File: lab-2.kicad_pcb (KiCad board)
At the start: 2 copper layers, 29.7 x 59.5 mm, 30 parts, among them J1 Conn_01x04_Pin, J2 USB_C_Receptacle, SW1 NRST, SW2 BOOT, U1 LM66100DCK, U2 LM66100DCK, U3 STM32F405RGTx, U4 MCP1700x-120xxMB, Y1 8 MHz

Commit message: Added 2 new layers + GPIO port A (4 pins)
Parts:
- added J3: Conn_PORT C, Connector_PinHeader_2.54mm:PinHeader_1x04_P2.54mm_Vertical, F.Cu at (170.3, 117.5)
- added J4: Conn_GND, Connector_PinHeader_2.54mm:PinHeader_1x04_P2.54mm_Vertical, F.Cu at (170.3, 90.8)
- J1: value Conn_01x04_Pin -> Conn_SWD
- turned U2 to -90 degrees
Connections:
- U3 pad 37: unconnected-(U3-PC6-Pad37) -> /GPIOC_6
- U3 pad 38: unconnected-(U3-PC7-Pad38) -> /GPIOC_7
- U3 pad 39: unconnected-(U3-PC8-Pad39) -> /GPIOC_8
- U3 pad 40: unconnected-(U3-PC9-Pad40) -> /GPIOC_9
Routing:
- net +3.3V: track 100.4 -> 22.5 mm, vias 0 -> 10
- net /GPIOC_9: track 0.00 -> 32.4 mm, vias 0 -> 2
- net /GPIOC_8: track 0.00 -> 28.1 mm, vias 0 -> 1
- net /GPIOC_7: track 0.00 -> 25.5 mm, vias 0 -> 2
- net /GPIOC_6: track 0.00 -> 22.1 mm, vias 0 -> 1
- net /SWCLK: track 22.9 -> 19.3 mm
- net +3.3V_STLINK: track 8.61 -> 6.46 mm
- net GND: track 38.0 -> 40.1 mm
- net +3.3V_LDO: track 15.0 -> 13.2 mm
- net /BOOT0: track 21.6 -> 20.6 mm, vias 2 -> 0
- net /SWDIO: track 17.3 -> 16.6 mm, vias 2 -> 0
- added copper zone on In2.Cu, net +3.3V
- added copper zone on In1.Cu, net GND
- removed copper zone on B.Cu, net GND
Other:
- copper layers 2 -> 4

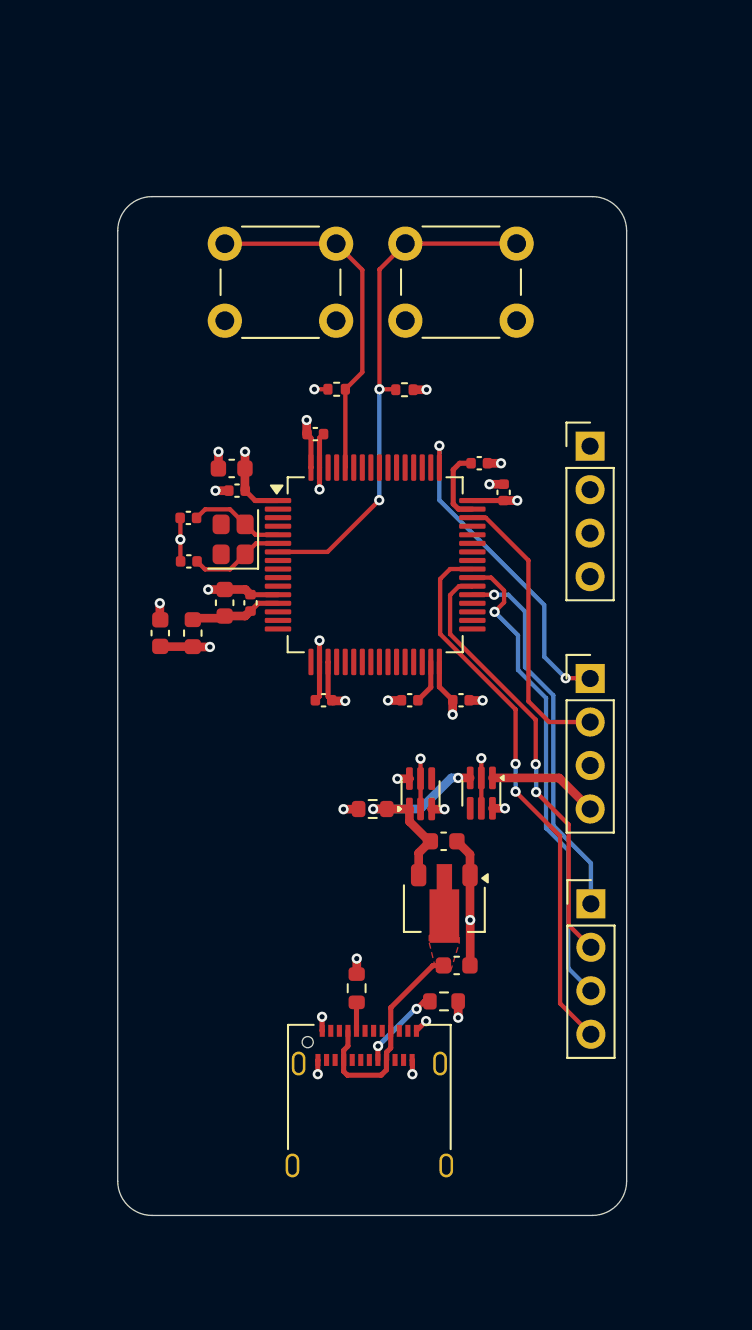
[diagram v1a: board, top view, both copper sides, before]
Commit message: add USER button and LEDs
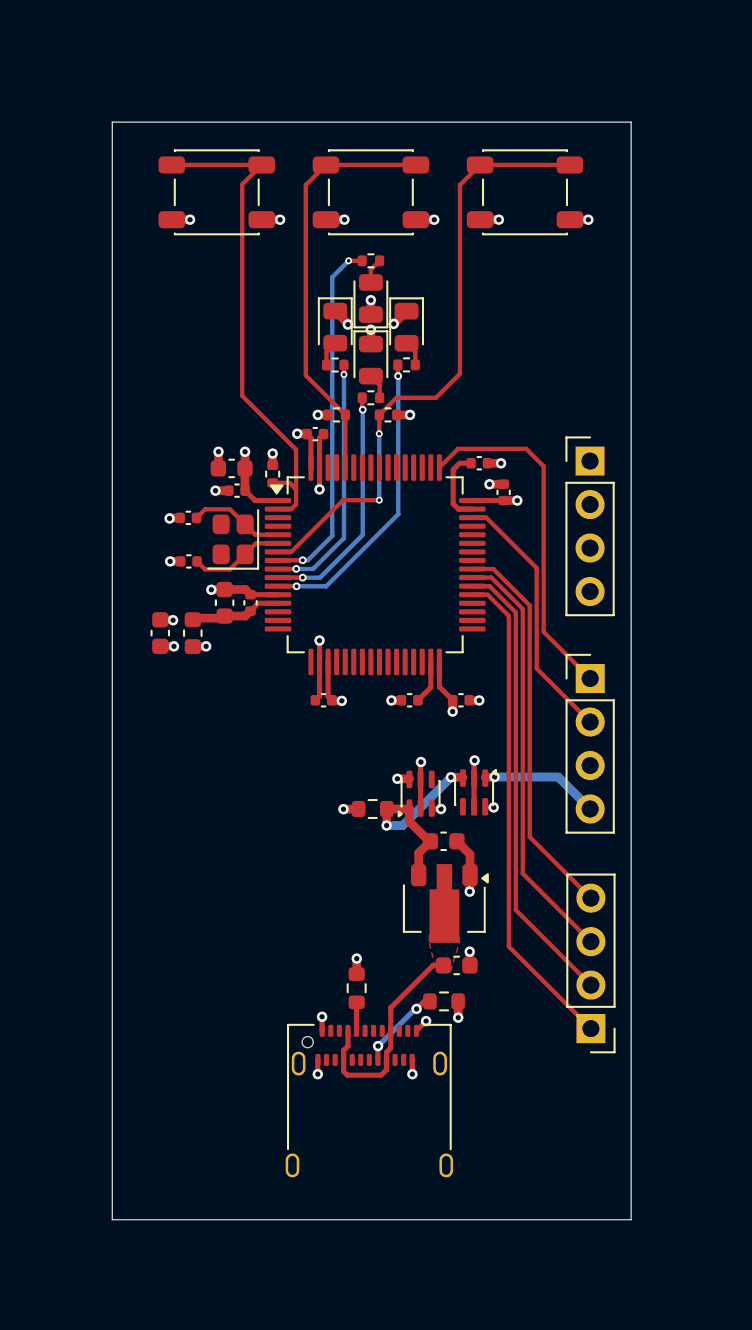
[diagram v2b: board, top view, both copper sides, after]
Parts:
- added D1: RED, LED_SMD:LED_0805_2012Metric, F.Cu at (157.5, 82.2)
- added D2: YELLOW, LED_SMD:LED_0805_2012Metric, F.Cu at (155.4, 83.9)
- added D3: GREEN, LED_SMD:LED_0805_2012Metric, F.Cu at (157.5, 85.8)
- added D4: BLUE, LED_SMD:LED_0805_2012Metric, F.Cu at (159.6, 83.9)
- added R10: 39, Resistor_SMD:R_0402_1005Metric, F.Cu at (159.6, 86.1)
- added R4: 130, Resistor_SMD:R_0402_1005Metric, F.Cu at (157.5, 80.0)
- added R7: 10k, Resistor_SMD:R_0402_1005Metric, F.Cu at (151.8, 92.5)
- added R8: 130, Resistor_SMD:R_0402_1005Metric, F.Cu at (155.4, 86.1)
- added R9: 56, Resistor_SMD:R_0402_1005Metric, F.Cu at (157.5, 88.0)
- added SW3: USER, Button_Switch_SMD:SW_SPST_PTS647_Sx38, F.Cu at (148.5, 76.0)
- SW1, SW2: footprint Button_Switch_THT:SW_PUSH_6mm_H4.3mm -> Button_Switch_SMD:SW_SPST_PTS647_Sx38
- moved SW2 9.04 mm to (157.5, 76.0)
- moved SW1 7.60 mm to (166.5, 76.0)
- moved J3 7.29 mm to (170.3, 124.8), turned to 180 degrees
- moved R5 1.76 mm to (158.5, 89.0)
- moved R6 1.50 mm to (155.5, 89.0)
- moved J4 0.87 mm to (170.3, 91.7)
- moved U2 0.43 mm to (163.5, 111.0)
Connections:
- U3 pad 10: unconnected-(U3-PC2-Pad10) -> /GREEN_LED
- U3 pad 11: unconnected-(U3-PC3-Pad11) -> /BLUE_LED
- U3 pad 2: unconnected-(U3-PC13-Pad2) -> /USER
- U3 pad 8: unconnected-(U3-PC0-Pad8) -> /RED_LED
- U3 pad 9: unconnected-(U3-PC1-Pad9) -> /YELLOW_LED
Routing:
- net /USER: track 0.00 -> 29.5 mm
- net /RED_LED: track 0.00 -> 21.0 mm, vias 0 -> 2
- net /BLUE_LED: track 0.00 -> 17.4 mm, vias 0 -> 2
- net /YELLOW_LED: track 0.00 -> 14.7 mm, vias 0 -> 2
- net /GREEN_LED: track 0.00 -> 14.0 mm, vias 0 -> 2
- net /GPIOC_9: track 32.4 -> 22.8 mm, vias 2 -> 0
- net /GPIOC_6: track 22.1 -> 28.7 mm, vias 1 -> 0
- net /NRST: track 30.2 -> 35.9 mm
- net /BOOT0: track 20.6 -> 24.4 mm
- net /GPIOC_8: track 28.1 -> 24.8 mm, vias 1 -> 0
- net +3.3V: track 22.5 -> 24.3 mm, vias 10 -> 15
- net Net-(D2-A): track 0.00 -> 1.49 mm
- net Net-(D4-A): track 0.00 -> 1.47 mm
- net Net-(D3-A): track 0.00 -> 1.47 mm
- net Net-(D1-A): track 0.00 -> 1.47 mm
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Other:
- board size 29.7 x 59.5 mm -> 30.3 x 64.1 mm

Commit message: added potentiometer
Signed-off-by: Yehor Bilous <bilous801@gmail.com>
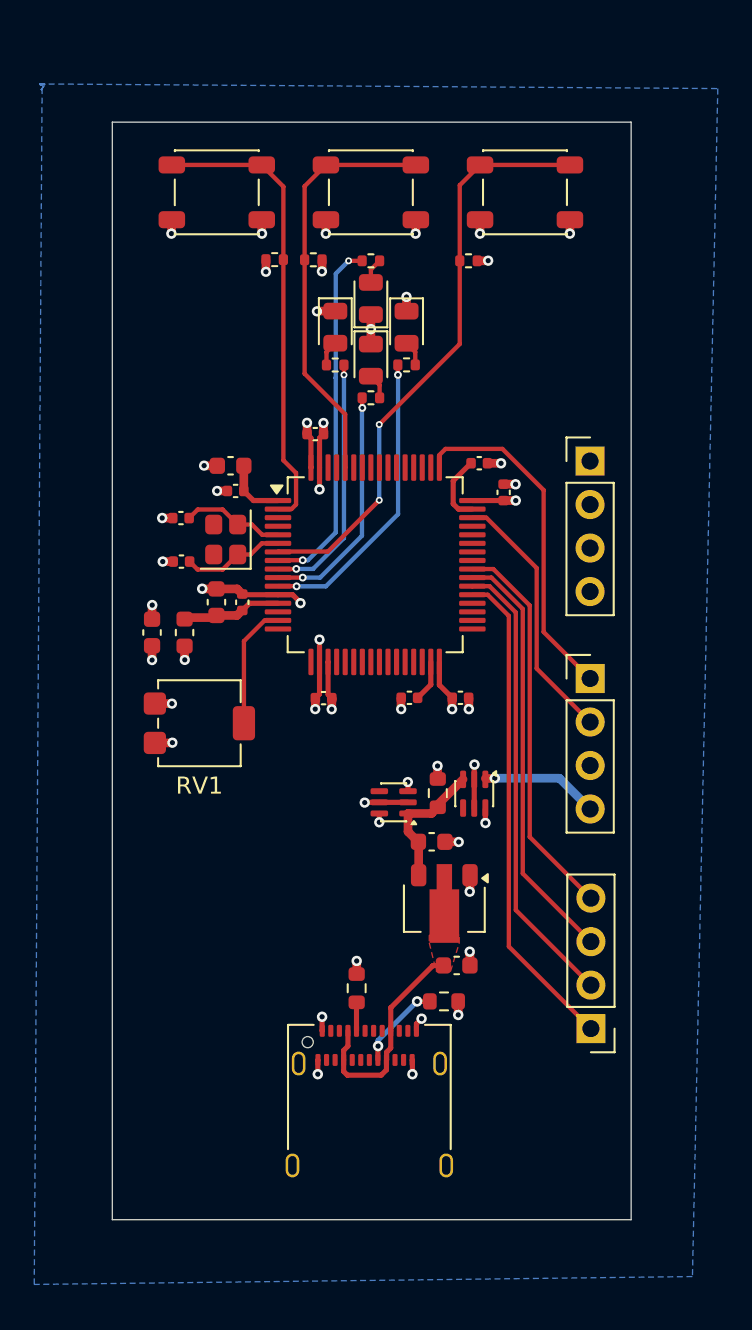
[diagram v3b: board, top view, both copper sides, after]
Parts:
- added RV1: R_Potentiometer_Small, Potentiometer_SMD:Potentiometer_Bourns_3224G_Horizontal, F.Cu at (147.5, 107.0)
- moved R7 12.5 mm to (151.9, 79.9), turned to 180 degrees
- moved R5 10.2 mm to (163.2, 80.0)
- moved R6 9.16 mm to (154.1, 79.9), turned to 0 degrees
- moved R3 3.91 mm to (161.4, 111.1), turned to -90 degrees
- moved U1 1.65 mm to (158.8, 111.6), turned to 180 degrees
- moved C10 0.70 mm to (161.1, 113.9)
- moved C6 0.48 mm to (150.0, 99.9)
- moved C8 0.48 mm to (144.7, 101.7)
- moved FB1 0.48 mm to (146.6, 101.7)
- moved C7 0.48 mm to (148.5, 99.9)
- moved C11 0.43 mm to (146.4, 95.0)
- moved Y1 0.43 mm to (149.0, 96.3)
- moved C12 0.43 mm to (146.4, 97.6)
- moved C0 0.17 mm to (149.3, 92.0)
- moved C5 0.15 mm to (162.7, 105.5)
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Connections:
- U3 pad 15: unconnected-(U3-PA1-Pad15) -> /POT_ADC
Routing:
- net /POT_ADC: track 0.00 -> 7.29 mm
- net +3.3V_LDO: track 12.6 -> 8.02 mm, vias 2 -> 0
- net /USER: track 29.5 -> 27.1 mm
- net /NRST: track 35.9 -> 34.4 mm
- net GND: track 41.0 -> 42.1 mm, vias 31 -> 35
- net +3.3V: track 24.3 -> 23.5 mm
- added copper zone on B.Cu, net GND

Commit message: fix some ERC and DRC issues
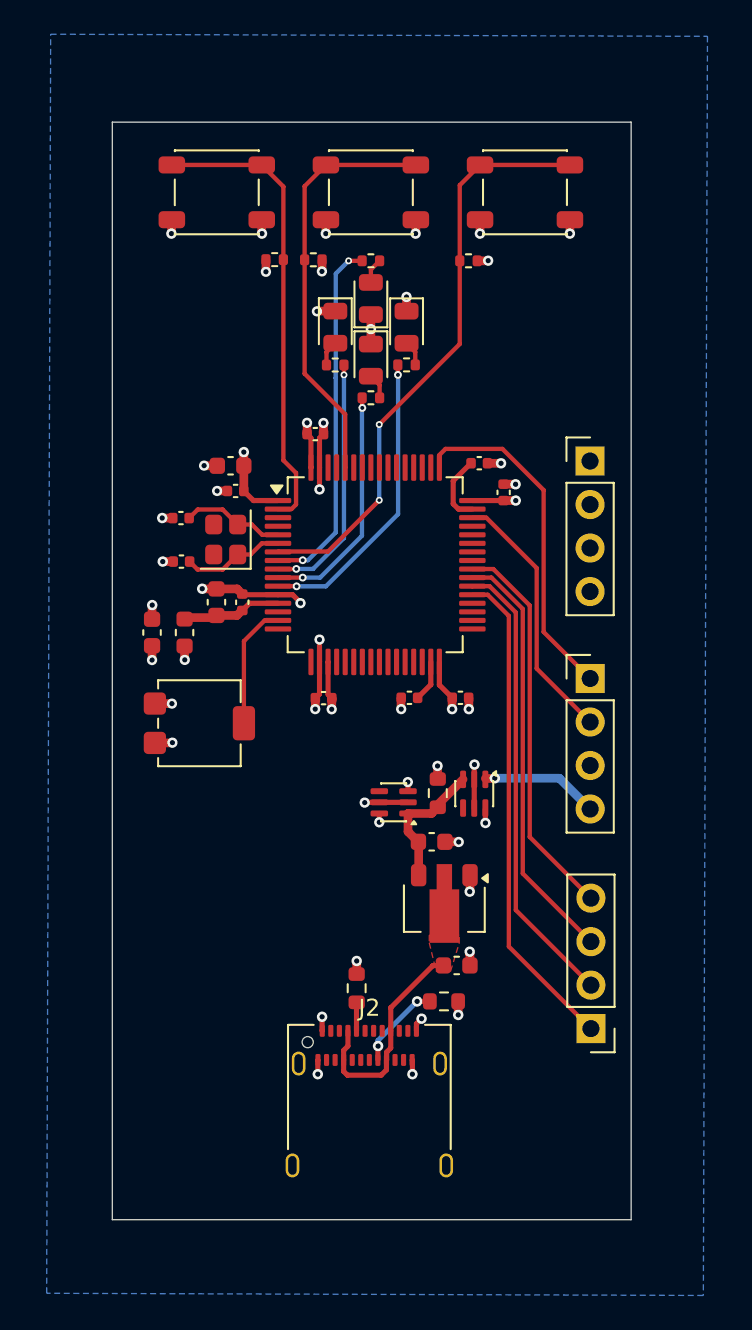
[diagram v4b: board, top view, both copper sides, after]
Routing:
- net +3.3V: track 23.5 -> 24.3 mm, vias 15 -> 16
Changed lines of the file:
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@@
 		(property "Reference" "RV1"
 			(at 0 -3.65 0)
-			(layer "F.SilkS")
+			(layer "F.Fab")
 			(effects
 				(font
-					(size 1 1)
-					(thickness 0.15)
+					(size 0.508 0.508)
+					(thickness 0.0762)
 				)
 			)
@@
 			(effects
 				(font
-					(size 1 1)
-					(thickness 0.15)
+					(size 0.508 0.508)
+					(thickness 0.0762)
 				)
 			)
@@
 			(effects
 				(font
-					(size 1.27 1.27)
+					(size 0.508 0.508)
+					(thickness 0.0762)
 				)
 			)
@@
 			(effects
 				(font
-					(size 1.27 1.27)
+					(size 0.508 0.508)
+					(thickness 0.0762)
+				)
+			)
+		)
+		(property "Sim.Device" "R"
+			(at 0 0 180)
+			(unlocked yes)
+			(layer "F.Fab")
+			(hide yes)
+			(effects
+				(font
+					(size 1 1)
+					(thickness 0.15)
+				)
+			)
+		)
+		(property "Sim.Type" "POT"
+			(at 0 0 180)
+			(unlocked yes)
+			(layer "F.Fab")
+			(hide yes)
+			(effects
+				(font
+					(size 1 1)
+					(thickness 0.15)
+				)
+			)
+		)
+		(property "Sim.Pins" "1=r0 2=wiper 3=r1"
+			(at 0 0 180)
+			(unlocked yes)
+			(layer "F.Fab")
+			(hide yes)
+			(effects
+				(font
+					(size 1 1)
+					(thickness 0.15)
 				)
 			)
@@
 			(effects
 				(font
-					(size 1 1)
-					(thickness 0.15)
+					(size 0.508 0.508)
+					(thickness 0.0762)
 				)
 			)
@@
 		(property "Reference" "J2"
 			(at 0 -6.36 0)
-			(layer "F.Fab")
+			(layer "F.SilkS")
 			(effects
 				(font
-					(size 0.508 0.508)
-					(thickness 0.0762)
+					(size 1 1)
+					(thickness 0.15)
 				)
 			)
@@
 			(effects
 				(font
-					(size 0.508 0.508)
-					(thickness 0.0762)
+					(size 1 1)
+					(thickness 0.15)
 				)
 			)
@@
 			(effects
 				(font
-					(size 0.508 0.508)
-					(thickness 0.0762)
+					(size 1.27 1.27)
+					(thickness 0.15)
 				)
 			)
@@
 			(effects
 				(font
-					(size 0.508 0.508)
-					(thickness 0.0762)
+					(size 1.27 1.27)
+					(thickness 0.15)
 				)
 			)
@@
 			(unit
 				(name "A")
-				(pins "S1" "B1" "B12" "A1" "A12" "B9" "A9" "B4" "A4" "A5" "B5" "A7" "B7"
+				(pins "SH" "B1" "B12" "A1" "A12" "B9" "A9" "B4" "A4" "A5" "B5" "A7" "B7"
 					"A6" "B6" "B10" "B11" "A3" "A2" "A10" "A11" "B3" "B2" "A8" "B8"
 				)
@@
 			(effects
 				(font
-					(size 0.508 0.508)
-					(thickness 0.0762)
+					(size 1 1)
+					(thickness 0.1)
 				)
 			)
@@
 			(remove_unused_layers no)
 			(net "GND")
+			(pinfunction "SHIELD_SH")
+			(pintype "passive")
 		)
 		(pad "SH" thru_hole oval
@@
 			(remove_unused_layers no)
 			(net "GND")
+			(pinfunction "SHIELD_SH")
+			(pintype "passive")
 		)
 		(pad "SH" thru_hole oval
@@
 			(remove_unused_layers no)
 			(net "GND")
+			(pinfunction "SHIELD_SH")
+			(pintype "passive")
 		)
 		(pad "SH" thru_hole oval
@@
 			(remove_unused_layers no)
 			(net "GND")
+			(pinfunction "SHIELD_SH")
+			(pintype "passive")
 		)
 		(embedded_fonts no)
@@
 	)
 	(segment
+		(start 150.08 91.1692)
+		(end 150.08 91.97)
+		(width 0.508)
+		(layer "F.Cu")
+		(net "+3.3V")
+	)
+	(segment
 		(start 154.87 77.605)
 		(end 154.875 77.6)
@@
 	)
 	(via
+		(at 150.08 91.1692)
+		(size 0.6096)
+		(drill 0.3048)
+		(layers "F.Cu" "B.Cu")
+		(net "+3.3V")
+	)
+	(via
 		(at 159.66 110.44)
 		(size 0.6)
@@
 	)
 	(segment
+		(start 150.085 102.211724)
+		(end 150.085 107.005)
+		(width 0.254)
+		(layer "F.Cu")
+		(net "/POT_ADC")
+	)
+	(segment
+		(start 151.296724 101)
+		(end 150.085 102.211724)
+		(width 0.254)
+		(layer "F.Cu")
+		(net "/POT_ADC")
+	)
+	(segment
+		(start 152.075 101)
+		(end 151.296724 101)
+		(width 0.254)
+		(layer "F.Cu")
+		(net "/POT_ADC")
+	)
+	(segment
 		(start 164.721 110.2325)
 		(end 164.7358 110.2177)
@@
 		(net "Net-(D1-A)")
 	)
-	(segment
-		(start 150.085 102.211724)
-		(end 150.085 107.005)
-		(width 0.254)
-		(layer "F.Cu")
-		(net "/POT_ADC")
-	)
-	(segment
-		(start 151.296724 101)
-		(end 150.085 102.211724)
-		(width 0.254)
-		(layer "F.Cu")
-		(net "/POT_ADC")
-	)
-	(segment
-		(start 152.075 101)
-		(end 151.296724 101)
-		(width 0.254)
-		(layer "F.Cu")
-		(net "/POT_ADC")
-	)
 	(zone
 		(net "+5V")
@@
 		(polygon
 			(pts
-				(xy 138.12 69.67) (xy 177.76 69.94) (xy 176.28 139.32) (xy 137.84 139.78) (xy 138.3 69.67) (xy 138.21 69.67)
-				(xy 138.21 69.76) (xy 138.21 69.67) (xy 138.21 69.76) (xy 138.3 69.69) (xy 138.37 69.81) (xy 138.23 70.03)
-				(xy 138.5 69.69)
+				(xy 177.156568 66.889647) (xy 176.915779 140.42378) (xy 138.565156 140.297062) (xy 138.799274 66.767516)
 			)
 		)
